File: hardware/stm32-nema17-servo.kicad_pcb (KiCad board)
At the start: 2 copper layers, 42 x 42 mm, 91 parts, among them J1 Conn_01x05, J2 C31-S-RA-CS1A-BK-SS, J3 TC-2050, J4 Screw_Terminal_01x02, J5 Screw_Terminal_01x02, J7 Conn_01x03, J8 Conn_01x03, J9 Conn_01x02, M1 Stepper_Motor_bipolar, Q1 NTTFS4937N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

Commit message: further fixes on v0.2 hardware
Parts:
- removed C7: 100n, Capacitor_SMD:C_0402_1005Metric
- removed U2: 74LVC2G32, Package_SON:X2SON-8_1.4x1mm_P0.35mm
- added R30: 10K, Resistor_SMD:R_0402_1005Metric, F.Cu at (163.8, 114.8)
- moved Q9 0.20 mm to (150.2, 100.9)
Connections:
- U1 pad 25: NSS -> (no net)
- U4 pad 1: ASCS -> ASEL
- U6 pad 32: DRVCS -> DRVSEL
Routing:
- net ASCS: track 37.1 -> 0.00 mm, vias 2 -> 0
- net ASEL: track 5.16 -> 37.8 mm, vias 0 -> 2
- net DRVCS: track 26.6 -> 0.00 mm, vias 2 -> 0
- net DRVSEL: track 7.56 -> 32.9 mm, vias 2 -> 4
- net NSS: track 7.84 -> 0.00 mm, vias 2 -> 0
- net SLCK: track 39.9 -> 36.1 mm
- net MISO: track 38.7 -> 36.7 mm
- net MOSI: track 39.5 -> 37.6 mm
- net VBUSDIV: track 50.3 -> 48.9 mm
- net GND: track 101.3 -> 100.1 mm, vias 52 -> 50
- net SCL3: track 17.5 -> 17.0 mm
- net +3V3: track 55.9 -> 56.4 mm

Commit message: hardware version 0.2 as sent to board fab
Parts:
- added C25: 10u 60V, Capacitor_SMD:C_1210_3225Metric, F.Cu at (156.0, 133.9)
- added C7: 10u 60V, Capacitor_SMD:C_1210_3225Metric, F.Cu at (166.8, 128.4)
- added D5: 3.3V 1mA, Diode_SMD:D_0402_1005Metric, F.Cu at (164.5, 113.5)
- added R31: 22K, Resistor_SMD:R_0402_1005Metric, F.Cu at (166.4, 116.0)
- added R32: 5K, Resistor_SMD:R_0402_1005Metric, F.Cu at (165.4, 116.0)
- moved C23 10.8 mm to (139.9, 133.9)
- moved C24 7.21 mm to (147.9, 133.9)
- moved C8 4.00 mm to (137.6, 110.8)
- moved J4 4.00 mm to (172.0, 130.1)
- moved J5 4.00 mm to (128.0, 110.0)
- moved Q1 4.00 mm to (133.8, 113.2)
- moved R6 4.00 mm to (136.1, 112.7)
- moved U3 4.00 mm to (138.6, 113.2)
- moved C14 2.37 mm to (159.8, 128.9), turned to 270 degrees
- moved Q7 2.02 mm to (160.1, 138.1)
- moved Q2 2.00 mm to (139.9, 138.1)
- moved Q3 2.00 mm to (144.0, 138.1)
- moved Q4 2.00 mm to (147.9, 138.1)
- moved Q5 2.00 mm to (152.0, 138.1)
- moved Q6 1.99 mm to (156.0, 138.1)
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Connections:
- U1 pad 25: (no net) -> DRVSEL
- U1 pad 29: DRVSEL -> (no net)
- U1 pad 38: (no net) -> VDDDIV
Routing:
- net VDDDIV: track 0.00 -> 22.7 mm, vias 0 -> 2
- net VBUS: track 15.2 -> 22.8 mm, vias 34 -> 47
- net +3V3: track 56.4 -> 52.2 mm
- net PWMR: track 16.0 -> 20.0 mm
- net GND: track 100.1 -> 104.1 mm, vias 50 -> 57
- net Net-(Q5-Pad4): track 13.8 -> 17.7 mm
- net VDD: track 100.2 -> 102.9 mm, vias 8 -> 9
- net RB: track 15.7 -> 17.9 mm
- net Net-(Q7-Pad4): track 20.8 -> 22.8 mm
- net OC: track 23.0 -> 24.9 mm
- net DRVSEL: track 32.9 -> 31.0 mm
- net ASEL: track 37.8 -> 35.9 mm
- net Net-(Q6-Pad4): track 23.9 -> 25.7 mm
- net OB: track 16.3 -> 18.0 mm
- net Net-(Q4-Pad4): track 17.5 -> 19.3 mm
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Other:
- board size 42 x 42 mm -> 48 x 43.9 mm
- board text added: "STM32-NEMA17-SERVO V0.2 (c) 2019-09 dgulyas@inrobco.de"
- board text removed: "-"
- board text removed: "STM32-NEMA17-SERVO V0.2 (c) 2019-08 dgulyas@inrobco.de"

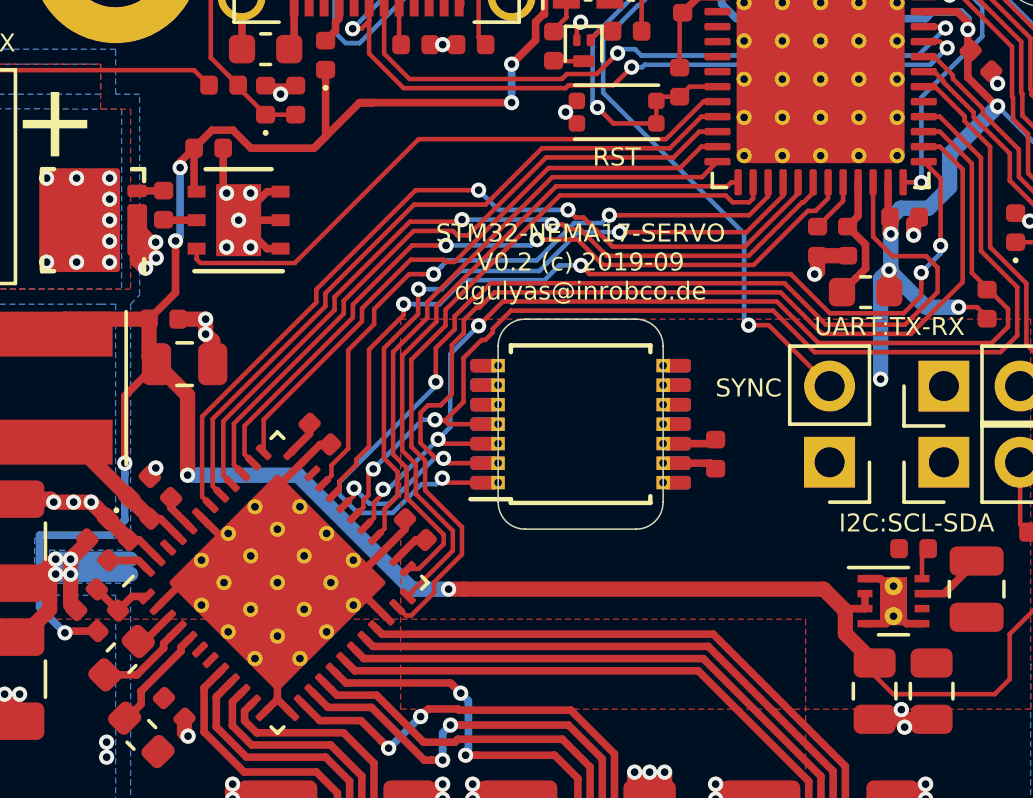
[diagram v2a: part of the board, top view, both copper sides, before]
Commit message: adds missing VREF connections on STM32 and DRV8323
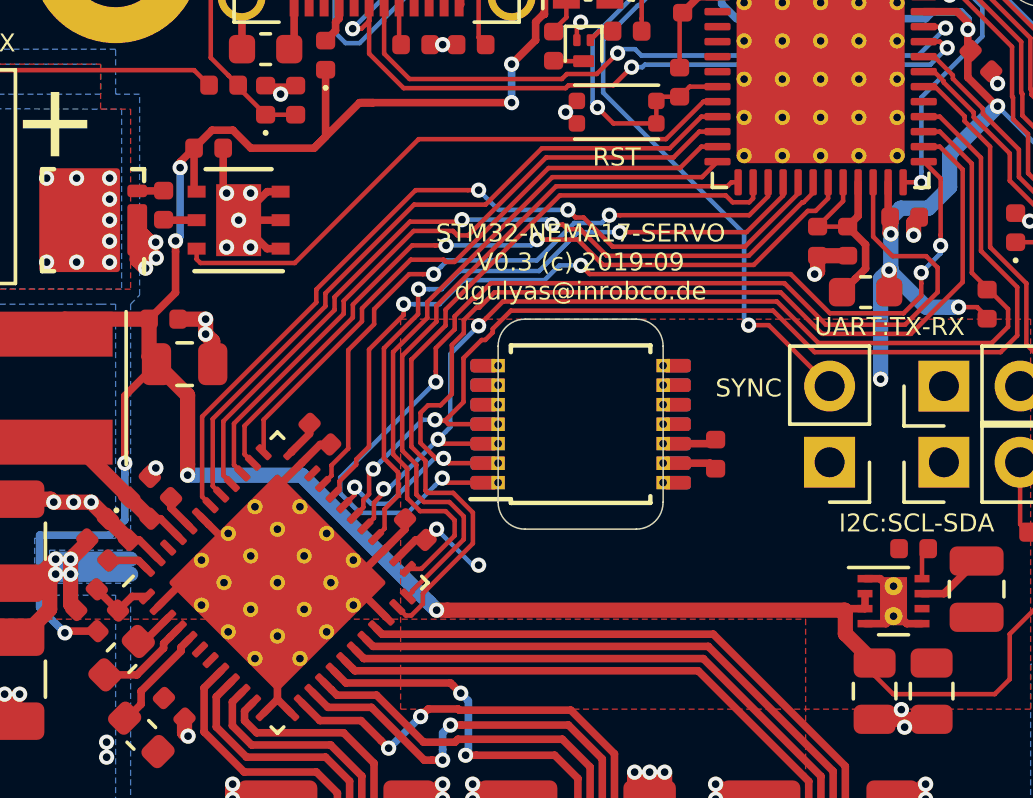
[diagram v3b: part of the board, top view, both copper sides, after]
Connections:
- C18 pad 1: Net-(C18-Pad1) -> +3V3
- C6 pad 1: Net-(C6-Pad1) -> +3.3VA
- U1 pad 20: Net-(C6-Pad1) -> +3.3VA
- U6 pad 26: Net-(C18-Pad1) -> +3V3
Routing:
- net +3V3: track 52.2 -> 55.8 mm, vias 10 -> 12
- net +3.3VA: track 4.38 -> 7.21 mm
- net Net-(C6-Pad1): track 1.83 -> 0.00 mm
- net Net-(C18-Pad1): track 1.20 -> 0.00 mm
- net SOA: track 22.4 -> 23.2 mm
- net SOB: track 23.2 -> 24.0 mm
- net SOC: track 25.2 -> 26.0 mm
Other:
- board text added: "STM32-NEMA17-SERVO V0.3 (c) 2019-09 dgulyas@inrobco.de"
- board text removed: "STM32-NEMA17-SERVO V0.2 (c) 2019-09 dgulyas@inrobco.de"

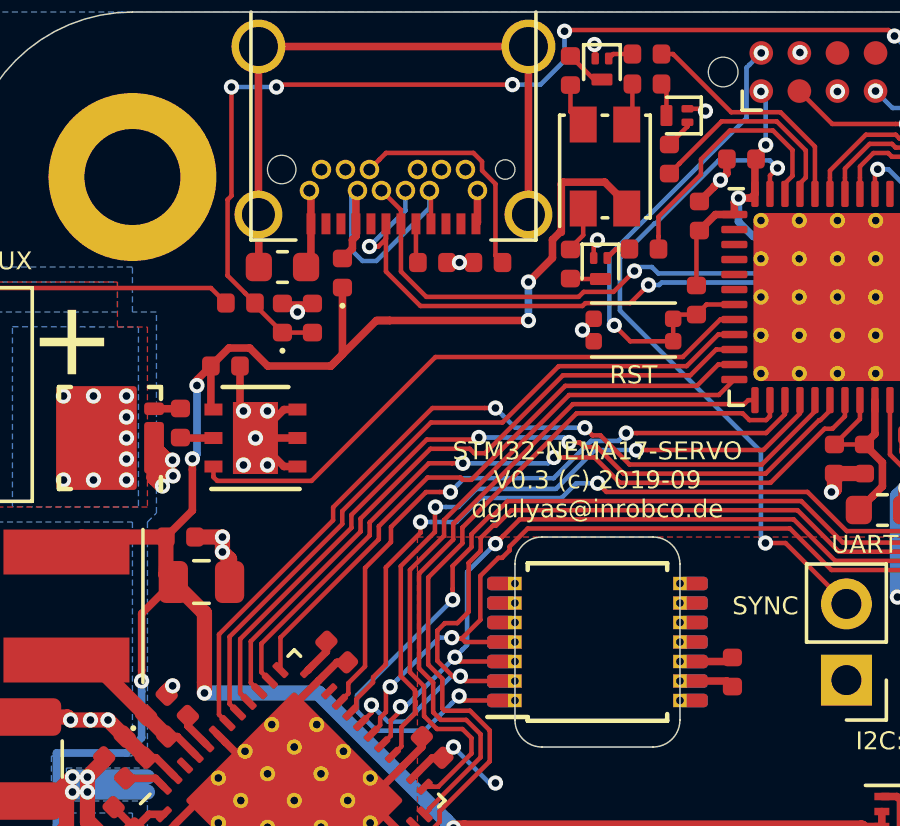
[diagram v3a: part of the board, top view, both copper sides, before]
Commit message: adds fuse to USB power input to protect both host and device
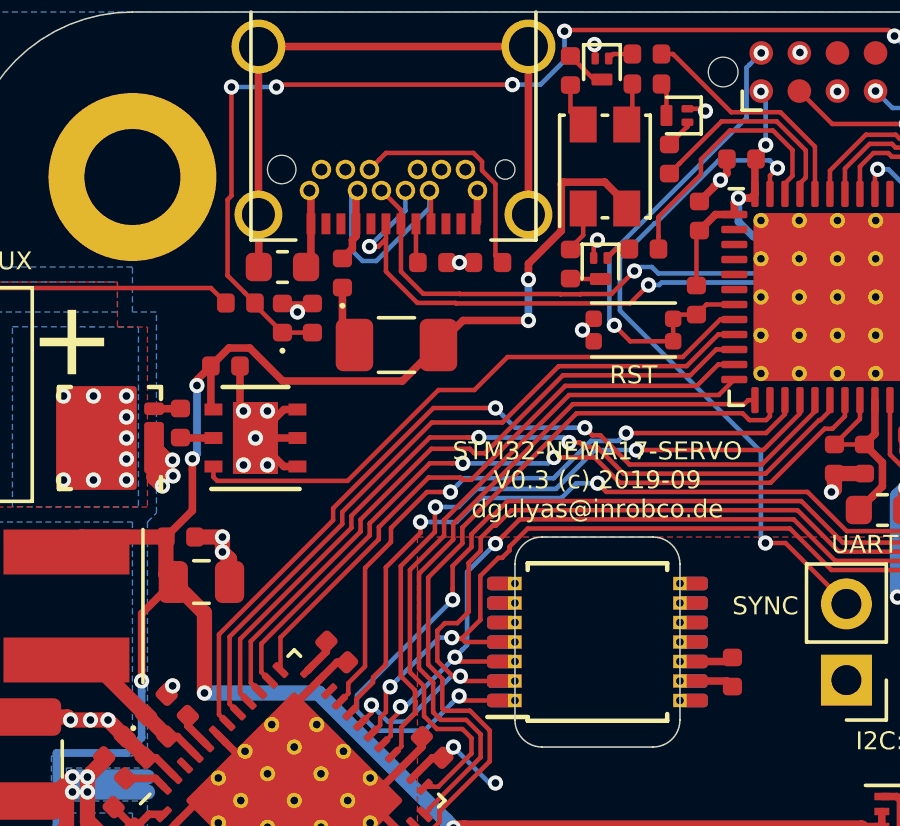
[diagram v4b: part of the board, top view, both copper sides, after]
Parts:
- added F1: 500mA, Fuse:Fuse_1206_3216Metric, F.Cu at (143.3, 110.1)
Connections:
- D1 pad 1: VDD -> Net-(D1-Pad1)
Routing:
- net VDD: track 102.9 -> 100.1 mm
- net Net-(D1-Pad1): track 0.00 -> 2.08 mm
- net DM: track 26.3 -> 25.7 mm

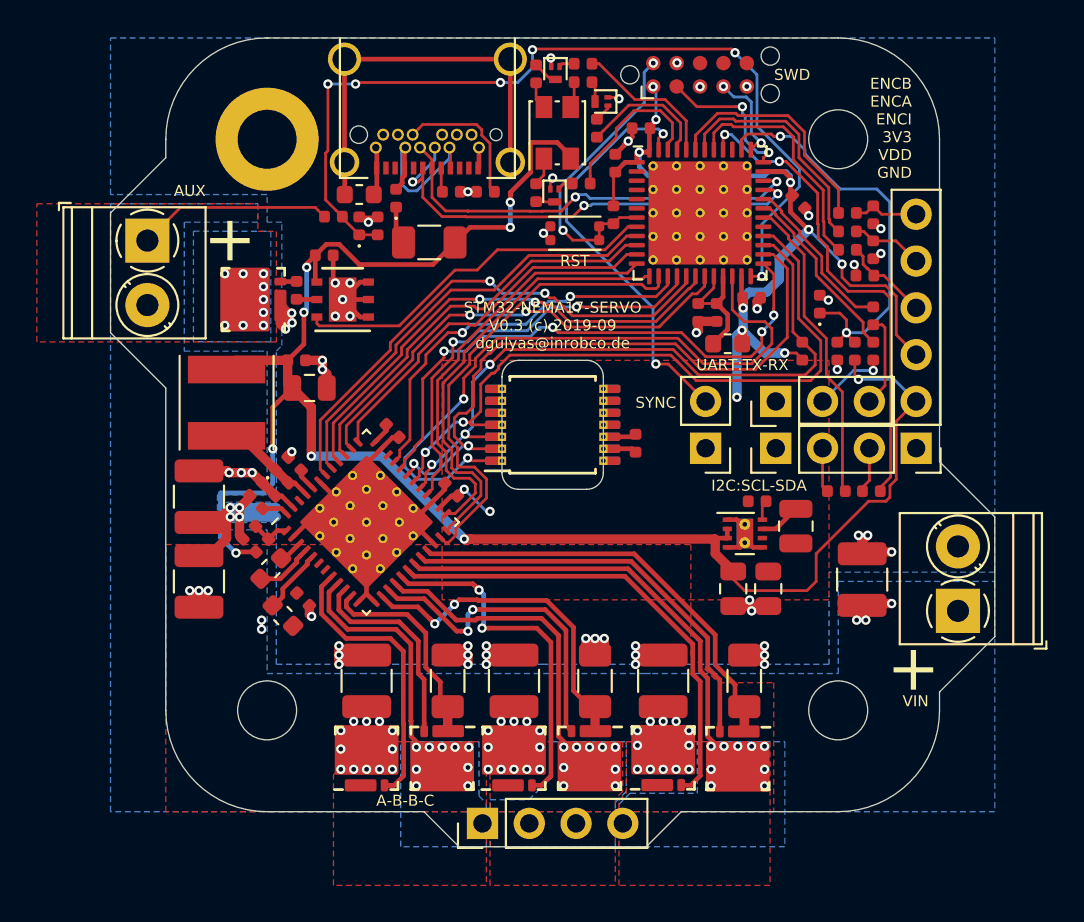
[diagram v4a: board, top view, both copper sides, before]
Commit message: software updated for V0.2 hardware, with characterization experiments; work on V0.3 hardware fixes
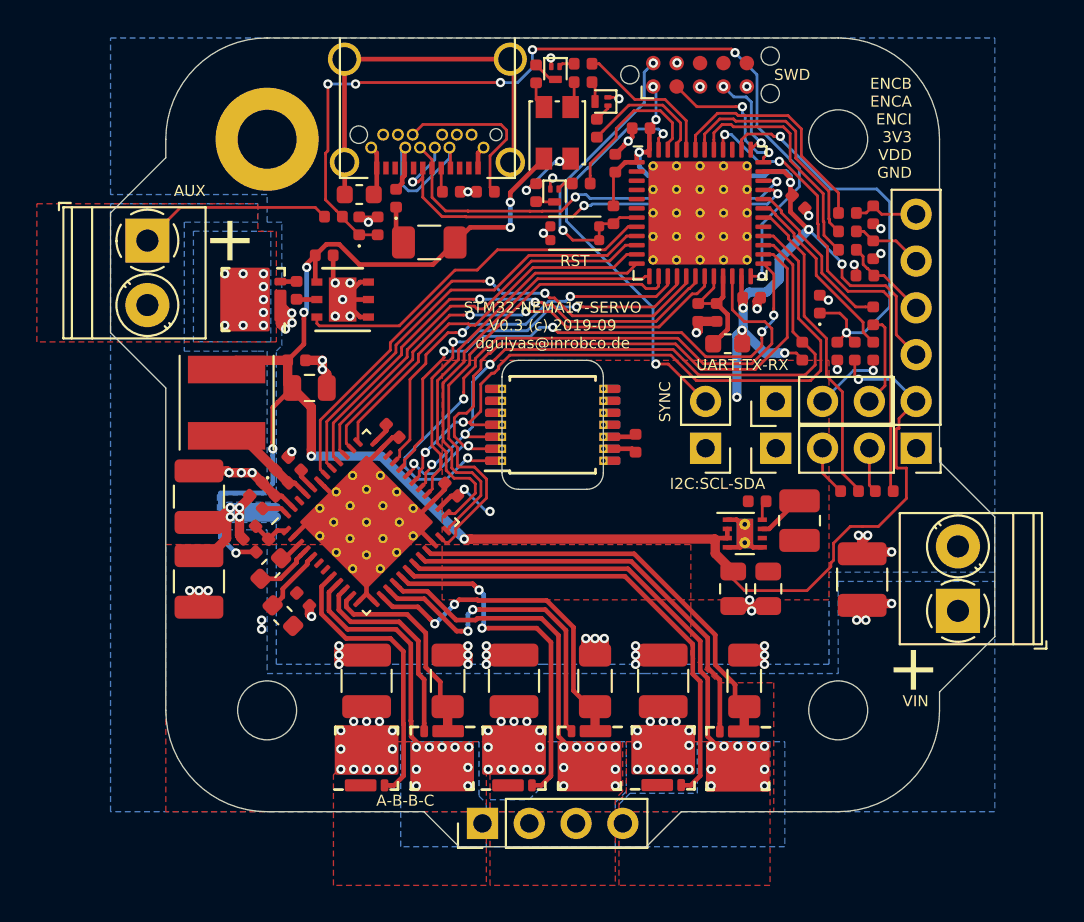
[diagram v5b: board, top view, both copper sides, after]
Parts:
- L2: footprint stm32-nema17:L_0806_2016Metric -> Inductor_SMD:L_1008_2520Metric
- R29, R32: value 5K -> 5.1K
- moved R25 0.72 mm to (166.1, 123.6)
- moved R26 0.70 mm to (168.0, 123.6)
- moved L2 0.36 mm to (163.4, 125.2)
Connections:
- D3 pad 1: Net-(D3-Pad1) -> VDD
- D3 pad 4: VDD -> Net-(D3-Pad4)
- J2 pad A8: (no net) -> Net-(J2-PadA8)
- J2 pad B8: (no net) -> Net-(J2-PadB8)
- J3 pad 6: (no net) -> Net-(J3-Pad6)
- J3 pad 7: (no net) -> Net-(J3-Pad7)
- J3 pad 8: (no net) -> Net-(J3-Pad8)
- R14 pad 2: LEDB -> LEDG
- R15 pad 2: LEDG -> LEDB
- R17 pad 1: Net-(D3-Pad1) -> Net-(D3-Pad4)
- U1 pad 2: (no net) -> Net-(U1-Pad2)
- U1 pad 29: (no net) -> Net-(U1-Pad29)
- U1 pad 3: (no net) -> Net-(U1-Pad3)
- U1 pad 39: (no net) -> Net-(U1-Pad39)
- U1 pad 4: (no net) -> Net-(U1-Pad4)
- U1 pad 44: LEDG -> LEDB
- U1 pad 46: LEDB -> LEDG
- U1 pad 5: (no net) -> Net-(U1-Pad5)
- U1 pad 6: (no net) -> Net-(U1-Pad6)
- U6 pad 34: (no net) -> Net-(U6-Pad34)
- U6 pad 46: (no net) -> Net-(U6-Pad46)
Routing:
- net Net-(D3-Pad4): track 0.00 -> 3.79 mm, vias 0 -> 2
- net VDD: track 100.1 -> 98.1 mm
- net Net-(J2-PadB5): track 7.75 -> 9.27 mm
- net Net-(D3-Pad1): track 1.49 -> 0.00 mm
- net LEDG: track 7.97 -> 8.86 mm
- net LEDB: track 8.86 -> 7.97 mm

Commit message: PCB layout improvements
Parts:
- D2: value 1A -> 1A 48V; footprint Diode_SMD:D_0402_1005Metric -> Diode_SMD:D_TUMD2
- Q1: value NTTFS4937N -> NVTFS5C658NL
- R29, R32: value 5.1K -> 5K1
- moved D2 2.17 mm to (136.0, 120.0), turned to 90 degrees
- moved C21 0.90 mm to (136.1, 115.6)
- moved C22 0.90 mm to (136.8, 117.1)
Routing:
- net /BUCK_SW: track 5.62 -> 7.67 mm
- net VDD: track 98.1 -> 99.3 mm
- net GND: track 104.3 -> 104.9 mm
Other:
- board text added: "STM32-NEMA17-SERVO V0.3 (c) 2020-03 dgulyas@inrobco.de"
- board text removed: "STM32-NEMA17-SERVO V0.3 (c) 2019-09 dgulyas@inrobco.de"

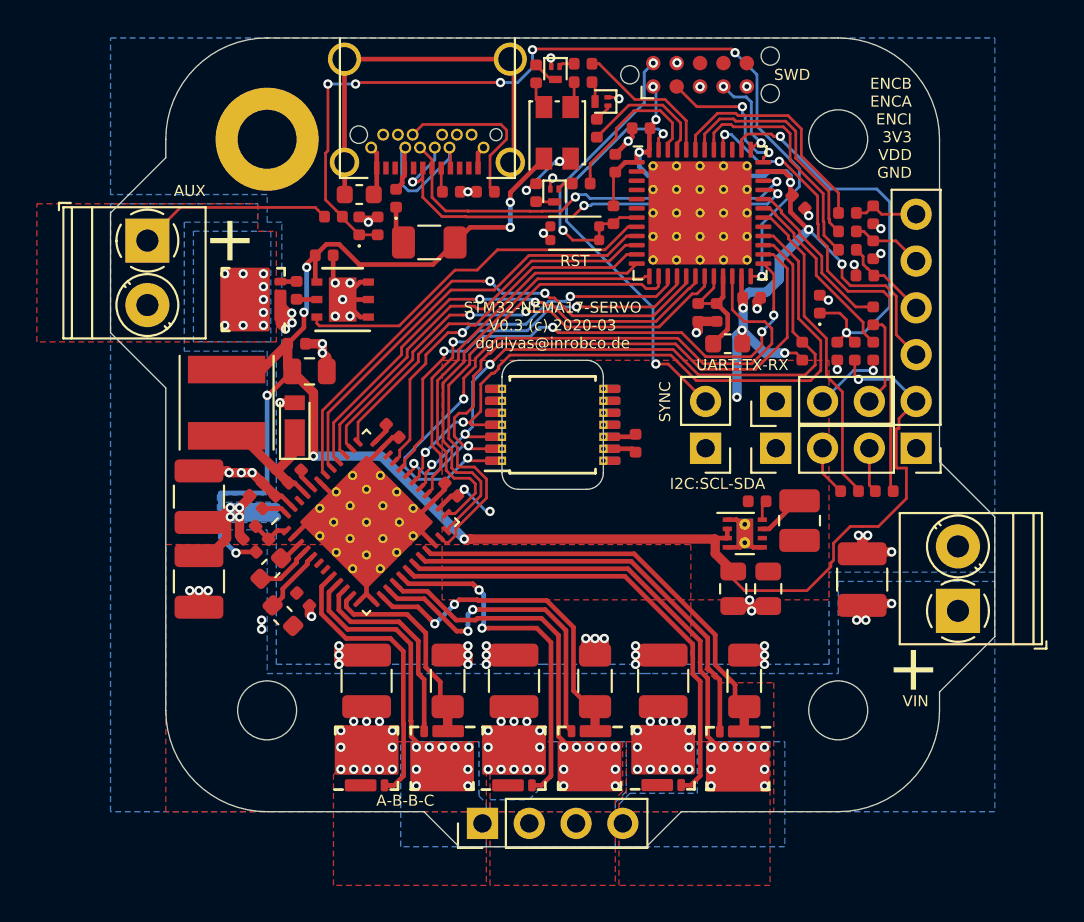
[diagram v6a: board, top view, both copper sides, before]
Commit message: more enhancements for v0.3, discovered that hardware NSS should be usable, after all
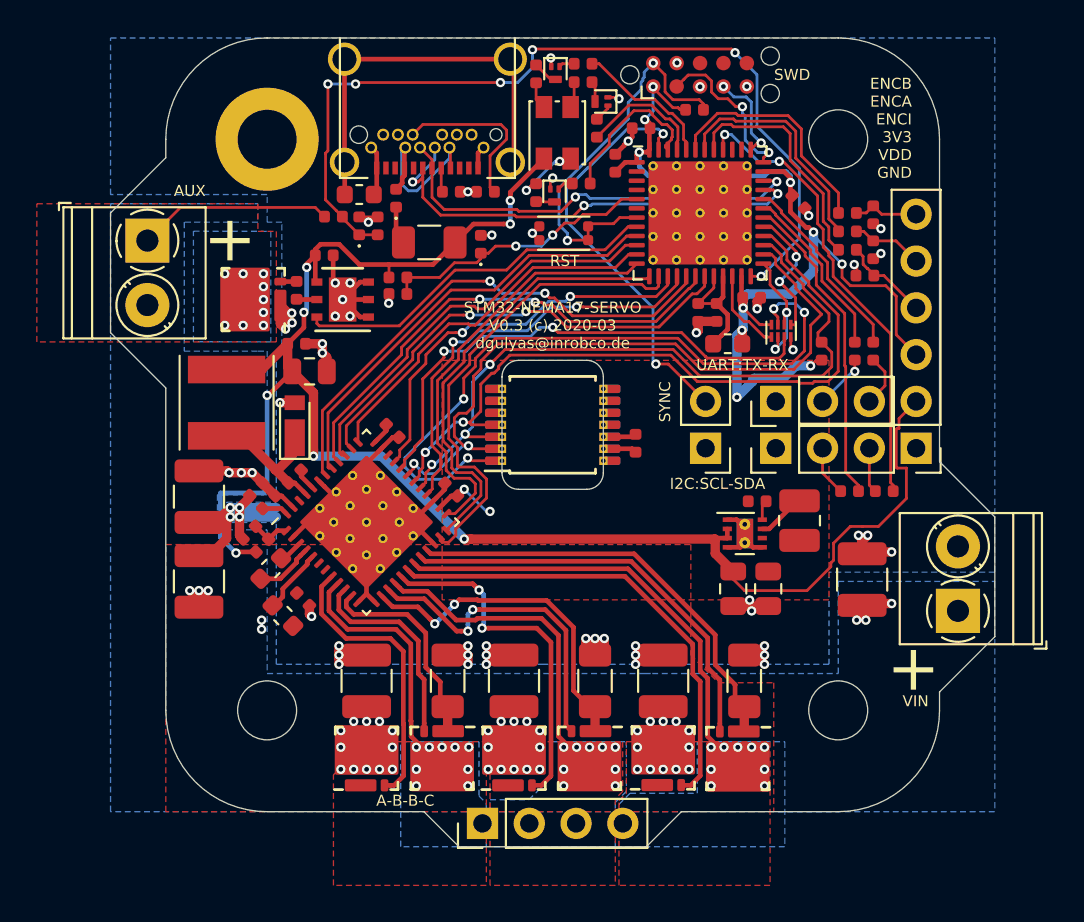
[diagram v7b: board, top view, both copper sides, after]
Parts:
- added U2: 74LVC2G32, Package_SON:X2SON-8_1.4x1mm_P0.35mm, F.Cu at (162.4, 114.9)
- moved R31 25.1 mm to (141.6, 112.0), turned to 0 degrees
- moved R32 24.1 mm to (141.6, 112.9), turned to 180 degrees
- moved D5 18.7 mm to (146.1, 110.2)
- moved R27 7.20 mm to (157.7, 102.9), turned to 180 degrees
- moved R24 1.92 mm to (167.4, 116.0)
- moved R30 1.05 mm to (164.6, 116.0)
- moved R23 1.00 mm to (166.4, 116.0)
- moved SW1 0.60 mm to (150.6, 109.6)
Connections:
- U1 pad 25: DRVSEL -> SPI_NSS
- U1 pad 29: Net-(U1-Pad29) -> DRVSEL
- U1 pad 38: VDDDIV -> Net-(U1-Pad38)
- U1 pad 5: Net-(U1-Pad5) -> VDDDIV
- U4 pad 1: ASEL -> A_NSS
- U6 pad 32: DRVSEL -> DRV_NSS
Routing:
- net A_NSS: track 0.00 -> 37.3 mm, vias 0 -> 4
- net ASEL: track 35.9 -> 4.55 mm, vias 2 -> 0
- net DRV_NSS: track 0.00 -> 28.0 mm, vias 0 -> 2
- net DRVSEL: track 31.0 -> 7.30 mm, vias 4 -> 2
- net VDDDIV: track 22.7 -> 15.3 mm
- net SPI_NSS: track 0.00 -> 6.87 mm, vias 0 -> 2
- net NRST: track 16.4 -> 21.2 mm
- net +3V3: track 55.8 -> 60.5 mm
- net VDD: track 99.3 -> 95.3 mm, vias 9 -> 8
- net SLCK: track 35.6 -> 38.3 mm
- net Net-(J7-Pad3): track 5.06 -> 2.86 mm
- net MISO: track 36.7 -> 38.8 mm
- net MOSI: track 37.5 -> 38.9 mm
- net RX1: track 9.08 -> 10.4 mm
- net SDA3: track 26.1 -> 25.0 mm
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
